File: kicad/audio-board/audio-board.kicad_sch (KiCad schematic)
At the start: 63 parts, among them J1 TO_CM5, J2 VBAT_IN, J3 A2B_TO_CUPS, U1 ADAU1861, U10 ADP7118AUJZ-3.3-R7, U2 ADXL354CEZ, U3 LTC6242, U4 IM72D128VV01, U5 AD2428WBCPZ, U6 SN74LVC8T245PWR, U7 SN74LVC8T245PWR, U8 PCA9517ADP, U9 ADP7118AUJZ-1.8-R7

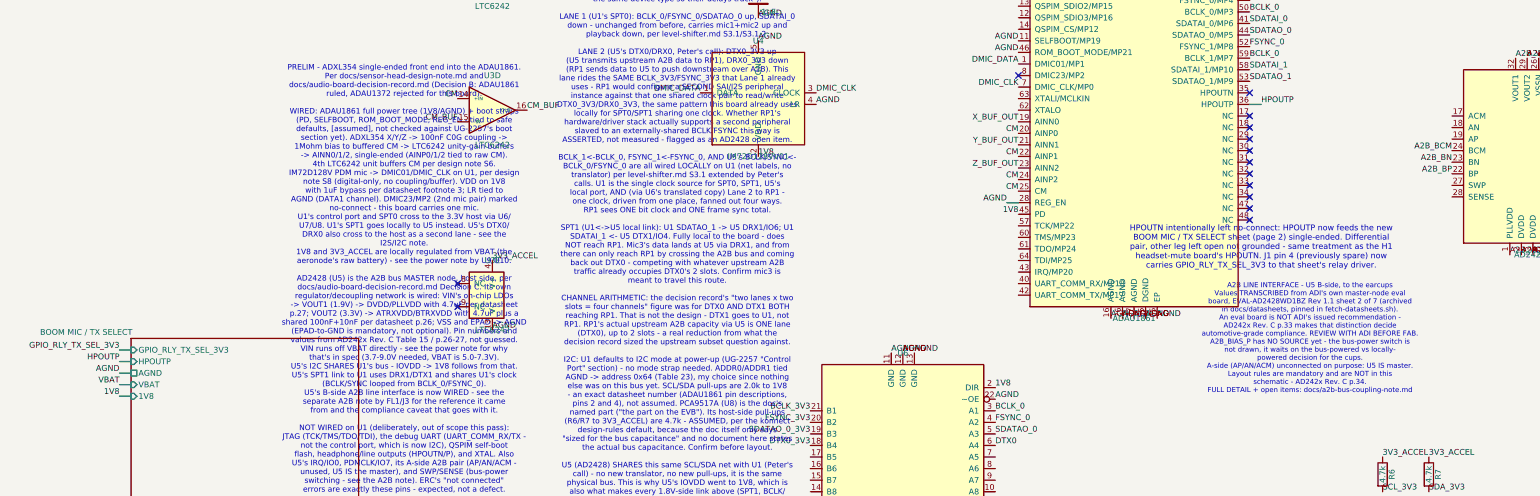
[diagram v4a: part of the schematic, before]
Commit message: [LIMA] add T1 (SM-LP-5001) for aircraft-side isolation, per Peter - replaces the C37/R13/D2-only network
Resolves the TRS ring/sleeve isolation question, and corrects a
mistake from two commits ago: the C37/R13/D2 network added for
HPOUTP protection cited the H1 headset-mute board's section 10.1,
but 10.1 was already superseded on that same board by its own
section 11 ("use the transformer approach for the aircraft side"),
which survives there only as a bench expedient. Missed that the
first time; caught reading the full H1 note before touching this
again.

Presented the tradeoff (H1's own §24-26 found the original ground-
loop argument for a transformer dead once AeroNode floats on
battery in flight, but a transformer's isolation is unconditional
where a cap+R+clamp's protection is calculated) and Peter ruled the
transformer for this board too, matching what H1 kept.

Per H1's section 11.2 circuit exactly:
- T1 (Bourns SM-LP-5001, 600:600 1:1, same part H1 uses) now sits
  between the relay and the TRS jack. HPOUTP/HPOUTN drive its
  primary directly and DIFFERENTIALLY through K1's two poles (both
  poles now used, not just pole A) - no DC to block, so C37 is
  gone entirely, and the "is the HP amp specified to run one leg
  unloaded" question closes because it no longer arises.
- R13 moved from the primary to the secondary (net MIC_LINE),
  per H1's explicit rule: an attenuator on the primary drags the
  LF corner into the voice band (419Hz for 10k into the 3.8H
  primary); on the secondary it sees only ~115R winding DCR (~5Hz).
- The secondary's other leg is a new net, AC_GND - the aircraft mic
  ground (J5 Sleeve) - explicitly separate from this board's AGND.
  Sleeve no longer bonds to AeroNode ground anywhere on this sheet.
- D2 (BAT54S) kept as belt-and-braces insurance per H1's own framing,
  now clamping HPOUTP directly rather than a node downstream of the
  removed C37/R13.

Generic Device:Transformer_1P_1S symbol used for T1, same as H1 -
its own note alr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
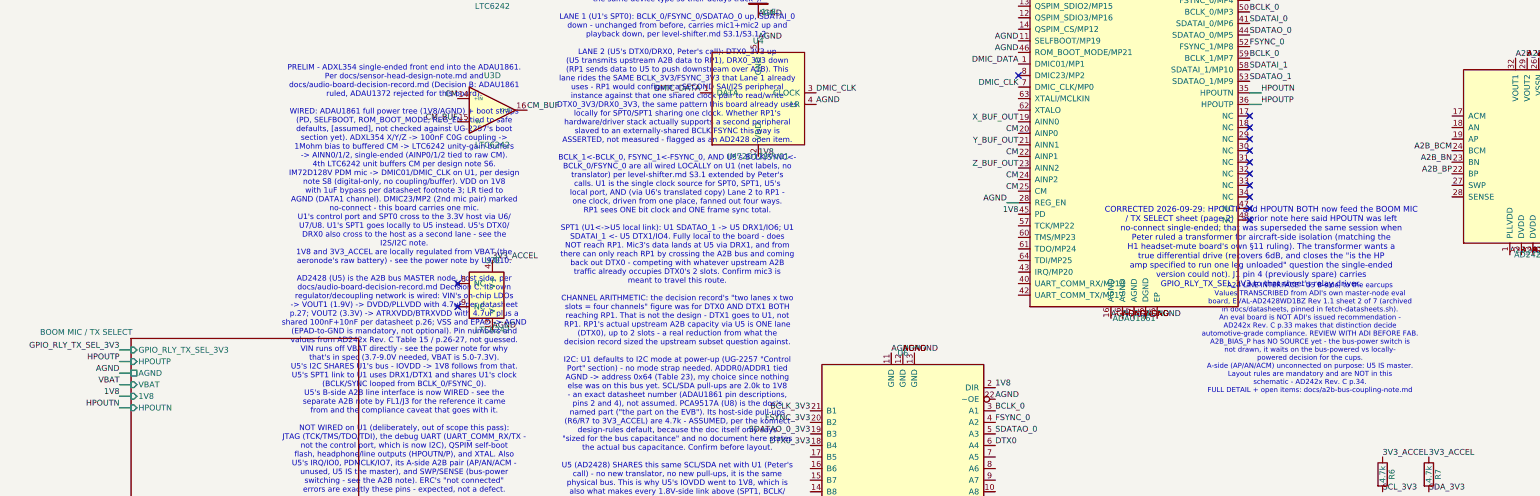
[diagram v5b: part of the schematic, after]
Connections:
- net HPOUTN: now reaches U1.35 (HPOUTN)
- no-connect marks 15 -> 14
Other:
- sheet BOOM MIC / TX SELECT ports: added HPOUTN; removed none
- note added: "CORRECTED 2026-09-29: HPOUTP and HPOUTN BOTH now feed the BOOM MIC / TX SELECT sheet (page 2) - a prior note here said HPOUTN was left no-connect single-ended; that was superseded the same session when Peter ruled a transformer for aircraft-side isolation (matching the H1 headset-mute board's own §11 ruling). The transformer wants a true differential drive (recovers 6dB, and closes the "is the HP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"
- note removed: "HPOUTN intentionally left no-connect: HPOUTP now feeds the new BOOM MIC / TX SELECT sheet (page 2) single-ended. Differential pair, other leg left open not grounded - same treatment as the H1 headset-mute board's HPOUTN. J1 pin 4 (previously spare) now carries GPIO_RLY_TX_SEL_3V3 to that sheet's relay driver."
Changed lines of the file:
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@@
 		(at 234.95 142.24)
-	)
-	(no_connect
-		(at 285.75 146.05)
 	)
 	(wire
@@
 		)
 	)
+	(wire
+		(pts
+			(xy 285.75 146.05)
+			(xy 288.29 146.05)
+		)
+	)
+	(wire
+		(pts
+			(xy 40 215.24)
+			(xy 37.46 215.24)
+		)
+	)
 	(text "Power in: VBAT from the aeronode board (U9/U10, J2). This\nis the ONLY supply arriving on this board - Peter confirmed\nno 3.3V rail comes over from the CM5 side at all.\n\nVBAT is aeronode's raw 2S LiFePO4 pack net (ahead of its\ncharger/buck stage) - per\nkicad/aeronode/doc/ARCHITECTURE.md: \"the pack never falls\nbelow 5.0V\" and \"the pack sits at 7.2V\" at full charge, so\nVBAT runs 5.0-7.3V. Fetched from that doc, not assumed.\nJ2 is a generic 2-pin placeholder for the board-to-board\nlink, same treatment as J1 for the CM5 - the actual\ninterconnect between aeronode and this board is undesigned.\n\nU9 = ADP7118AUJZ-1.8-R7 -> 1V8. U10 = ADP7118AUJZ-3.3-R7\n-> 3V3_ACCEL. NOT the ADP1715 the EVAL-ADAU1860 uses for\nthe same two rails (docs/rig-logic-levels.md) - that part\nis 2.5-5.5V in and VBAT hits 7.3V, over its max. ADP7118\nis the same family's wide-input sibling, 2.7-20V, comfortably\ncovering VBAT with margin. Pin numbers and the EN/SENSE\nwiring (EN->VIN for auto-start, SENSE/ADJ->VOUT for the\nfixed-voltage grade, both from datasheet Table 4/Fig. 1)\nare from the datasheet, not guessed. 2.2uF on each VIN and\nVOUT per the datasheet's own minimum.\n\n1V8 and 3V3_ACCEL no longer carry a PWR_FLAG - they have a\nreal local source now. VBAT gets the PWR_FLAG instead,\nsince it is the new board-boundary net.\n\nCORRECTED THIS PASS: there is no separate \"3V3_CM5\" rail\narriving from the CM5 side - Peter confirmed only VBAT\ncrosses the board boundary. The net previously called\n3V3_CM5 (VCCB for U6/U7, VCC(B)/EN for U8, R6/R7's pull-up\nreference, and a J1 pin) has been MERGED into 3V3_ACCEL -\nU10 is now the single 3.3V source for the accelerometer AND\nthe whole host-facing translator stack (U6, U7, U8, R6, R7).\nThe old 3V3_CM5 PWR_FLAG and its J1 pin are both removed;\nJ1 pins 4 and 8 are both spare now. RP1 does not need to\nsupply this board's 3.3V logic-level reference - its own\nGPIO bank has its own 3.3V rail, and U10's independently-\ngenerated 3.3V is close enough (both \"3.3V nominal\") for\nthe translators and repeater to interoperate correctly,\nthe same way any two boards with separate 3.3V supplies and\na shared ground normally do.\n\nOPEN, sharpened by the merge: U10 (ADP7118, 200mA/rail) now\ncarries the accelerometer's own supply AND both I2S\ntranslators' VCCB AND the I2C repeater's VCC(B)/EN AND two\n4.7k pull-ups. Still almost certainly well inside 200mA,\nbut this is now a real aggregate worth computing before\nlayout, not just \"the accelerometer's load.\" Board-to-board\nconnector for VBAT unresolved, same as J1. No transient/\ninrush check has been done for U9, U10, and U5's on-chip\nregulator sharing one VBAT feed through J2."
 		(at 100 50 0)
@@
 		)
 	)
-	(text "HPOUTN intentionally left no-connect: HPOUTP now feeds the new\nBOOM MIC / TX SELECT sheet (page 2) single-ended. Differential\npair, other leg left open not grounded - same treatment as the H1\nheadset-mute board's HPOUTN. J1 pin 4 (previously spare) now\ncarries GPIO_RLY_TX_SEL_3V3 to that sheet's relay driver."
-		(at 288.29 180 0)
-		(effects
-			(font
-				(size 1.27 1.27)
-			)
-		)
-	)
 	(label "X_ACCEL_OUT"
 		(at 72.39 88.9 0)
@@
 	(label "1V8"
 		(at 37.46 212.7 180)
+		(effects
+			(font
+				(size 1.27 1.27)
+			)
+			(justify right bottom)
+		)
+	)
+	(label "HPOUTN"
+		(at 288.29 146.05 0)
+		(effects
+			(font
+				(size 1.27 1.27)
+			)
+			(justify left bottom)
+		)
+	)
+	(label "HPOUTN"
+		(at 37.46 215.24 180)
 		(effects
 			(font
@@
 			(at 40 212.7 180)
 		)
+		(pin "HPOUTN" input
+			(at 40 215.24 180)
+		)
 		(instances
 			(project "audio-board"
@@
 		)
 	)
+  (text "CORRECTED 2026-09-29: HPOUTP and HPOUTN BOTH now feed the BOOM MIC\n/ TX SELECT sheet (page 2) - a prior note here said HPOUTN was left\nno-connect single-ended; that was superseded the same session when\nPeter ruled a transformer for aircraft-side isolation (matching the\nH1 headset-mute board's own §11 ruling). The transformer wants a\ntrue differential drive (recovers 6dB, and closes the \"is the HP\namp specified to run one leg unloaded\" question the single-ended\nversion could not). J1 pin 4 (previously spare) carries\nGPIO_RLY_TX_SEL_3V3 to that sheet's relay driver."
+    (at 288.29 180 0)
+    (effects (font (size 1.27 1.27)))
+  )
 	(symbol
 		(lib_id "AnalogDevices:ADAU1861")

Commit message: [LIMA] revert to single-ended HPOUTP + blocking cap, resize R13 to match the real mic, per Peter
Two changes from Peter, implemented together.

1. Single-ended drive, not differential. HPOUTN backed out (sheet
pin, hierarchical label, U1 wiring all reverted to no-connect); K1
pole B unused again. T1's primary is now HPOUTP (via K1 pole A) on
one leg, AGND fixed on the other. This needed a new capacitor, C38
(2.2uF) in series with HPOUTP - not for the old reason (blocking the
aircraft's 8-16V mic bias, which T1 already handles unconditionally)
but a different one: HPOUTP sits at the DAC's ~0.85V common-mode
bias, and grounding the primary's other leg directly would push
that DC across the winding continuously (~7.4mA toward core
saturation) without a cap in the way.

Checked the ADAU186x Hardware Reference Manual (UG-2257, cached in
this repo) on whether single-ended output is actually documented:
it isn't. The output stage is described as differential throughout,
and unlike the analog inputs (explicit single-ended mode + an
AINx_INPUT_MODE register bit), there is no equivalent output mode
in prose or in the HP_CTRL register. Recorded as a flagged residual,
not resolved by adding the cap - the cap fixes the DC problem, it
doesn't make this a specified configuration.

Also recorded a firmware-adjacent finding from the same manual:
HP_MODE (HP_CTRL bit 0) should be set to line-out (1), not the
headphone-mode (0) reset default - T1's primary presents 7-72k of
inductive reactance across the voice band, a line-out load, not a
headphone one (rated >=10 ohm) load.

2. R13 resized 10k -> 470R. It had been copied from the H1 board's
R1 without checking it against this mic. The already-fetched Bose
A20 reference (docs/h1-headset-mute-relay.md) gives the mic's own
source impedance as 220-2200 ohm (the bias resistor) - our path at
10k presented 20-40x that, and delivered only 35mV rms against the
mic's 600mV/114dB SPL rating. At 470R the presented impedance
(585R with T1's windi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
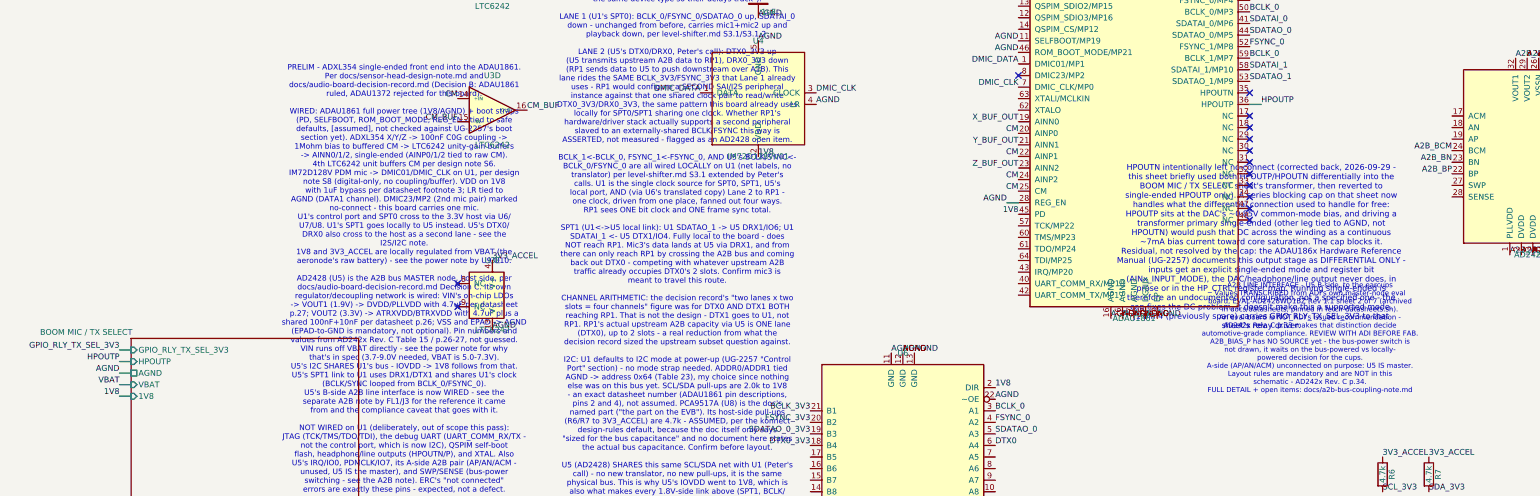
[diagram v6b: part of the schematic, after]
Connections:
- net HPOUTN: no longer names the net of U1.35 (HPOUTN)
- no-connect marks 14 -> 15
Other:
- sheet BOOM MIC / TX SELECT ports: added none; removed HPOUTN
- note added: "HPOUTN intentionally left no-connect (corrected back, 2026-09-29 - this sheet briefly used both HPOUTP/HPOUTN differentially into the BOOM MIC / TX SELECT sheet's transformer, then reverted to single-ended HPOUTP only). A series blocking cap on that sheet now handles what the differential connection used to handle for free: HPOUTP sits at the DAC's ~0.85V common-mode bias, and driving a transform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"
- note removed: "CORRECTED 2026-09-29: HPOUTP and HPOUTN BOTH now feed the BOOM MIC / TX SELECT sheet (page 2) - a prior note here said HPOUTN was left no-connect single-ended; that was superseded the same session when Peter ruled a transformer for aircraft-side isolation (matching the H1 headset-mute board's own §11 ruling). The transformer wants a true differential drive (recovers 6dB, and closes the "is the HP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"
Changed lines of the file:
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@@
 		(at 234.95 142.24)
+	)
+	(no_connect
+		(at 285.75 146.05)
 	)
 	(wire
@@
 		)
 	)
-	(wire
-		(pts
-			(xy 285.75 146.05)
-			(xy 288.29 146.05)
-		)
-	)
-	(wire
-		(pts
-			(xy 40 215.24)
-			(xy 37.46 215.24)
-		)
-	)
 	(text "Power in: VBAT from the aeronode board (U9/U10, J2). This\nis the ONLY supply arriving on this board - Peter confirmed\nno 3.3V rail comes over from the CM5 side at all.\n\nVBAT is aeronode's raw 2S LiFePO4 pack net (ahead of its\ncharger/buck stage) - per\nkicad/aeronode/doc/ARCHITECTURE.md: \"the pack never falls\nbelow 5.0V\" and \"the pack sits at 7.2V\" at full charge, so\nVBAT runs 5.0-7.3V. Fetched from that doc, not assumed.\nJ2 is a generic 2-pin placeholder for the board-to-board\nlink, same treatment as J1 for the CM5 - the actual\ninterconnect between aeronode and this board is undesigned.\n\nU9 = ADP7118AUJZ-1.8-R7 -> 1V8. U10 = ADP7118AUJZ-3.3-R7\n-> 3V3_ACCEL. NOT the ADP1715 the EVAL-ADAU1860 uses for\nthe same two rails (docs/rig-logic-levels.md) - that part\nis 2.5-5.5V in and VBAT hits 7.3V, over its max. ADP7118\nis the same family's wide-input sibling, 2.7-20V, comfortably\ncovering VBAT with margin. Pin numbers and the EN/SENSE\nwiring (EN->VIN for auto-start, SENSE/ADJ->VOUT for the\nfixed-voltage grade, both from datasheet Table 4/Fig. 1)\nare from the datasheet, not guessed. 2.2uF on each VIN and\nVOUT per the datasheet's own minimum.\n\n1V8 and 3V3_ACCEL no longer carry a PWR_FLAG - they have a\nreal local source now. VBAT gets the PWR_FLAG instead,\nsince it is the new board-boundary net.\n\nCORRECTED THIS PASS: there is no separate \"3V3_CM5\" rail\narriving from the CM5 side - Peter confirmed only VBAT\ncrosses the board boundary. The net previously called\n3V3_CM5 (VCCB for U6/U7, VCC(B)/EN for U8, R6/R7's pull-up\nreference, and a J1 pin) has been MERGED into 3V3_ACCEL -\nU10 is now the single 3.3V source for the accelerometer AND\nthe whole host-facing translator stack (U6, U7, U8, R6, R7).\nThe old 3V3_CM5 PWR_FLAG and its J1 pin are both removed;\nJ1 pins 4 and 8 are both spare now. RP1 does not need to\nsupply this board's 3.3V logic-level reference - its own\nGPIO bank has its own 3.3V rail, and U10's independently-\ngenerated 3.3V is close enough (both \"3.3V nominal\") for\nthe translators and repeater to interoperate correctly,\nthe same way any two boards with separate 3.3V supplies and\na shared ground normally do.\n\nOPEN, sharpened by the merge: U10 (ADP7118, 200mA/rail) now\ncarries the accelerometer's own supply AND both I2S\ntranslators' VCCB AND the I2C repeater's VCC(B)/EN AND two\n4.7k pull-ups. Still almost certainly well inside 200mA,\nbut this is now a real aggregate worth computing before\nlayout, not just \"the accelerometer's load.\" Board-to-board\nconnector for VBAT unresolved, same as J1. No transient/\ninrush check has been done for U9, U10, and U5's on-chip\nregulator sharing one VBAT feed through J2."
 		(at 100 50 0)
@@
 	(label "1V8"
 		(at 37.46 212.7 180)
-		(effects
-			(font
-				(size 1.27 1.27)
-			)
-			(justify right bottom)
-		)
-	)
-	(label "HPOUTN"
-		(at 288.29 146.05 0)
-		(effects
-			(font
-				(size 1.27 1.27)
-			)
-			(justify left bottom)
-		)
-	)
-	(label "HPOUTN"
-		(at 37.46 215.24 180)
 		(effects
 			(font
@@
 			(at 40 212.7 180)
 		)
-		(pin "HPOUTN" input
-			(at 40 215.24 180)
-		)
 		(instances
 			(project "audio-board"
@@
 		)
 	)
-  (text "CORRECTED 2026-09-29: HPOUTP and HPOUTN BOTH now feed the BOOM MIC\n/ TX SELECT sheet (page 2) - a prior note here said HPOUTN was left\nno-connect single-ended; that was superseded the same session when\nPeter ruled a transformer for aircraft-side isolation (matching the\nH1 headset-mute board's own §11 ruling). The transformer wants a\ntrue differential drive (recovers 6dB, and closes the \"is the HP\namp specified to run one leg unloaded\" question the single-ended\nversion could not). J1 pin 4 (previously spare) carries\nGPIO_RLY_TX_SEL_3V3 to that sheet's relay driver."
+  (text "HPOUTN intentionally left no-connect (corrected back, 2026-09-29 -\nthis sheet briefly used both HPOUTP/HPOUTN differentially into the\nBOOM MIC / TX SELECT sheet's transformer, then reverted to\nsingle-ended HPOUTP only). A series blocking cap on that sheet now\nhandles what the differential connection used to handle for free:\nHPOUTP sits at the DAC's ~0.85V common-mode bias, and driving a\ntransformer primary single-ended (other leg tied to AGND, not\nHPOUTN) would push that DC across the winding as a continuous\n~7mA bias current toward core saturation. The cap blocks it.\nResidual, not resolved by the cap: the ADAU186x Hardware Reference\nManual (UG-2257) documents this output stage as DIFFERENTIAL ONLY -\ninputs get an explicit single-ended mode and register bit\n(AINx_INPUT_MODE), the DAC/headphone/line output never does, in\nprose or in the HP_CTRL register map. Running single-ended is\ntherefore an undocumented configuration, not a specified one - the\ncap fixes the DC problem, it doesn't make this a supported mode.\nJ1 pin 4 (previously spare) carries GPIO_RLY_TX_SEL_3V3 to that\nsheet's relay driver."
     (at 288.29 180 0)
     (effects (font (size 1.27 1.27)))
